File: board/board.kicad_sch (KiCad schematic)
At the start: 34 parts, among them J1 Conn_01x25_Socket, J2 Conn_01x25_Socket, J5 PJ-320B, J6 Screw_Terminal_01x02, J7 Screw_Terminal_01x02, J8 Screw_Terminal_01x02

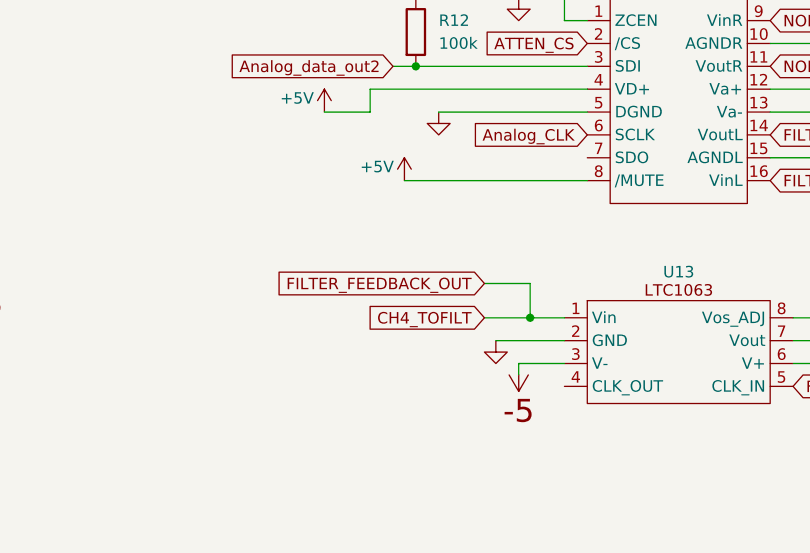
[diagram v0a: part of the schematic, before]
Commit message: connection successful message + add resistor to filter feedback loop
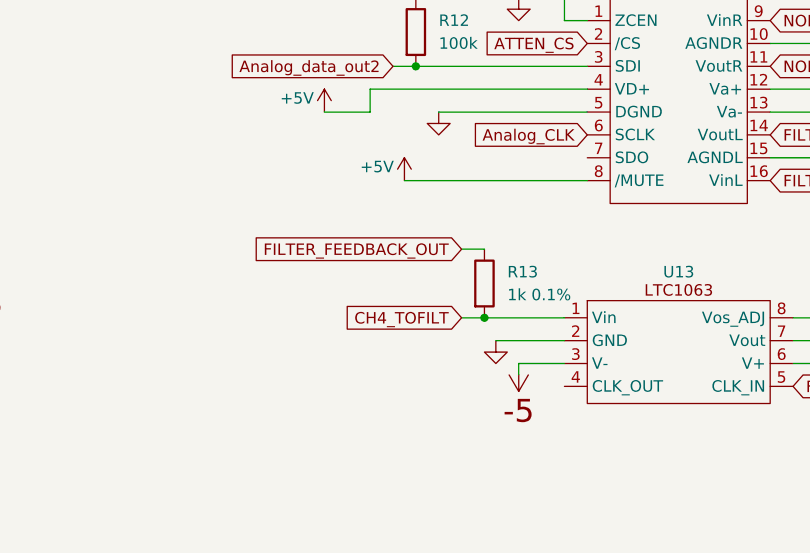
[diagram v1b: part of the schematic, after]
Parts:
- added R13: 1k_0603_0.1%, 4ms_Resistor:R_0603, symbol 4ms_Resistor:1k_0603_0.1%
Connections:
- net CH4_TOFILT: now also R13.2; no longer U10.14 (VoutL)
- new net FILTER_FEEDBACK_OUT: R13.1, U10.14 (VoutL)
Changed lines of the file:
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@@
 	)
 	(junction
-		(at 133.35 247.65)
-		(diameter 0)
-		(color 0 0 0 0)
-	)
-	(junction
 		(at 120.65 219.71)
 		(diameter 0)
@@
 	)
 	(junction
+		(at 128.27 247.65)
+		(diameter 0)
+		(color 0 0 0 0)
+	)
+	(junction
 		(at 229.87 236.22)
 		(diameter 0)
@@
 	(wire
 		(pts
-			(xy 128.27 247.65) (xy 133.35 247.65)
+			(xy 125.73 247.65) (xy 128.27 247.65)
 		)
 		(stroke
@@
 	(wire
 		(pts
+			(xy 128.27 247.65) (xy 137.16 247.65)
+		)
+		(stroke
+			(width 0)
+			(type default)
+		)
+	)
+	(wire
+		(pts
 			(xy 129.54 58.42) (xy 129.54 59.69)
 		)
@@
 	(wire
 		(pts
-			(xy 133.35 243.84) (xy 133.35 247.65)
-		)
-		(stroke
-			(width 0)
-			(type default)
-		)
-	)
-	(wire
-		(pts
 			(xy 82.55 175.26) (xy 82.55 177.8)
 		)
@@
 	(wire
 		(pts
-			(xy 133.35 247.65) (xy 137.16 247.65)
-		)
-		(stroke
-			(width 0)
-			(type default)
-		)
-	)
-	(wire
-		(pts
 			(xy 134.62 139.7) (xy 137.16 139.7)
 		)
@@
 	(wire
 		(pts
-			(xy 128.27 243.84) (xy 133.35 243.84)
+			(xy 125.73 240.03) (xy 128.27 240.03)
 		)
 		(stroke
@@
 	(global_label "CH4_TOFILT"
 		(shape input)
-		(at 128.27 247.65 180)
+		(at 125.73 247.65 180)
 		(fields_autoplaced yes)
 		(effects
@@
 		)
 		(property "Intersheetrefs" "${INTERSHEET_REFS}"
-			(at 114.52 247.65 0)
+			(at 111.98 247.65 0)
 			(effects
 				(font
@@
 	(global_label "FILTER_FEEDBACK_OUT"
 		(shape input)
-		(at 128.27 243.84 180)
+		(at 125.73 240.03 180)
 		(fields_autoplaced yes)
 		(effects
@@
 		)
 		(property "Intersheetrefs" "${INTERSHEET_REFS}"
-			(at 104.0577 243.84 0)
+			(at 101.5177 240.03 0)
 			(effects
 				(font
@@
 					(unit 1)
 				)
+			)
+		)
+	)
+	(symbol
+		(lib_id "4ms_Resistor:1k_0603_0.1%")
+		(at 128.27 243.84 0)
+		(unit 1)
+		(exclude_from_sim no)
+		(in_bom yes)
+		(on_board yes)
+		(dnp no)
+		(fields_autoplaced yes)
+		(property "Reference" "R13"
+			(at 130.81 242.5699 0)
+			(effects
+				(font
+					(size 1.27 1.27)
+				)
+				(justify left)
+			)
+		)
+		(property "Value" "1k_0603_0.1%"
+			(at 125.73 243.84 90)
+			(effects
+				(font
+					(size 1.27 1.27)
+				)
+				(hide yes)
+			)
+		)
+		(property "Footprint" "4ms_Resistor:R_0603"
+			(at 125.73 256.54 0)
+			(effects
+				(font
+					(size 1.27 1.27)
+				)
+				(justify left)
+				(hide yes)
+			)
+		)
+		(property "Datasheet" ""
+			(at 128.27 243.84 0)
+			(effects
+				(font
+					(size 1.27 1.27)
+				)
+				(hide yes)
+			)
+		)
+		(property "Description" "1k, 0.1%, 1/16W, 0603 25ppm"
+			(at 128.27 243.84 0)
+			(effects
+				(font
+					(size 1.27 1.27)
+				)
+				(hide yes)
+			)
+		)
+		(property "Display" "1k 0.1%"
+			(at 130.81 245.1099 0)
+			(effects
+				(font
+					(size 1.27 1.27)
+				)
+				(justify left)
+			)
+		)
+		(property "Specifications" "1k, 0.1%, 1/16W, 0603, 25ppm"
+			(at 125.73 251.714 0)
+			(effects
+				(font
+					(size 1.27 1.27)
+				)
+				(justify left)
+				(hide yes)
+			)
+		)
+		(property "Manufacturer" "Panasonic"
+			(at 125.73 253.238 0)
+			(effects
+				(font
+					(size 1.27 1.27)
+				)
+				(justify left)
+				(hide yes)
+			)
+		)
+		(property "Part Number" "ERA-3AEB102V"
+			(at 125.73 254.762 0)
+			(effects
+				(font
+					(size 1.27 1.27)
+				)
+				(justify left)
+				(hide yes)
+			)
+		)
+		(property "Manufacturer 2" "Yageo"
+			(at 126.365 258.445 0)
+			(effects
+				(font
+					(size 1.27 1.27)
+				)
+				(justify left)
+				(hide yes)
+			)
+		)
+		(property "Part Number 2" "RT0603BRD071KL"
+			(at 126.365 260.35 0)
+			(effects
+				(font
+					(size 1.27 1.27)
+				)
+				(justify left)
+				(hide yes)
+			)
+		)
+		(property "JLCPCB ID" "C54019"
+			(at 126.365 260.35 0)
+			(effects
+				(font
+					(size 1.27 1.27)
+				)
+				(justify left)
+				(hide yes)
+			)
+		)
+		(pin "1"
+		)
+		(pin "2"
+		)
+		(instances
+			(project "board"
+				(path "/e8cec806-e837-4d6f-b166-2de75a563bd6"
+					(reference "R13")
+					(unit 1)
+				)

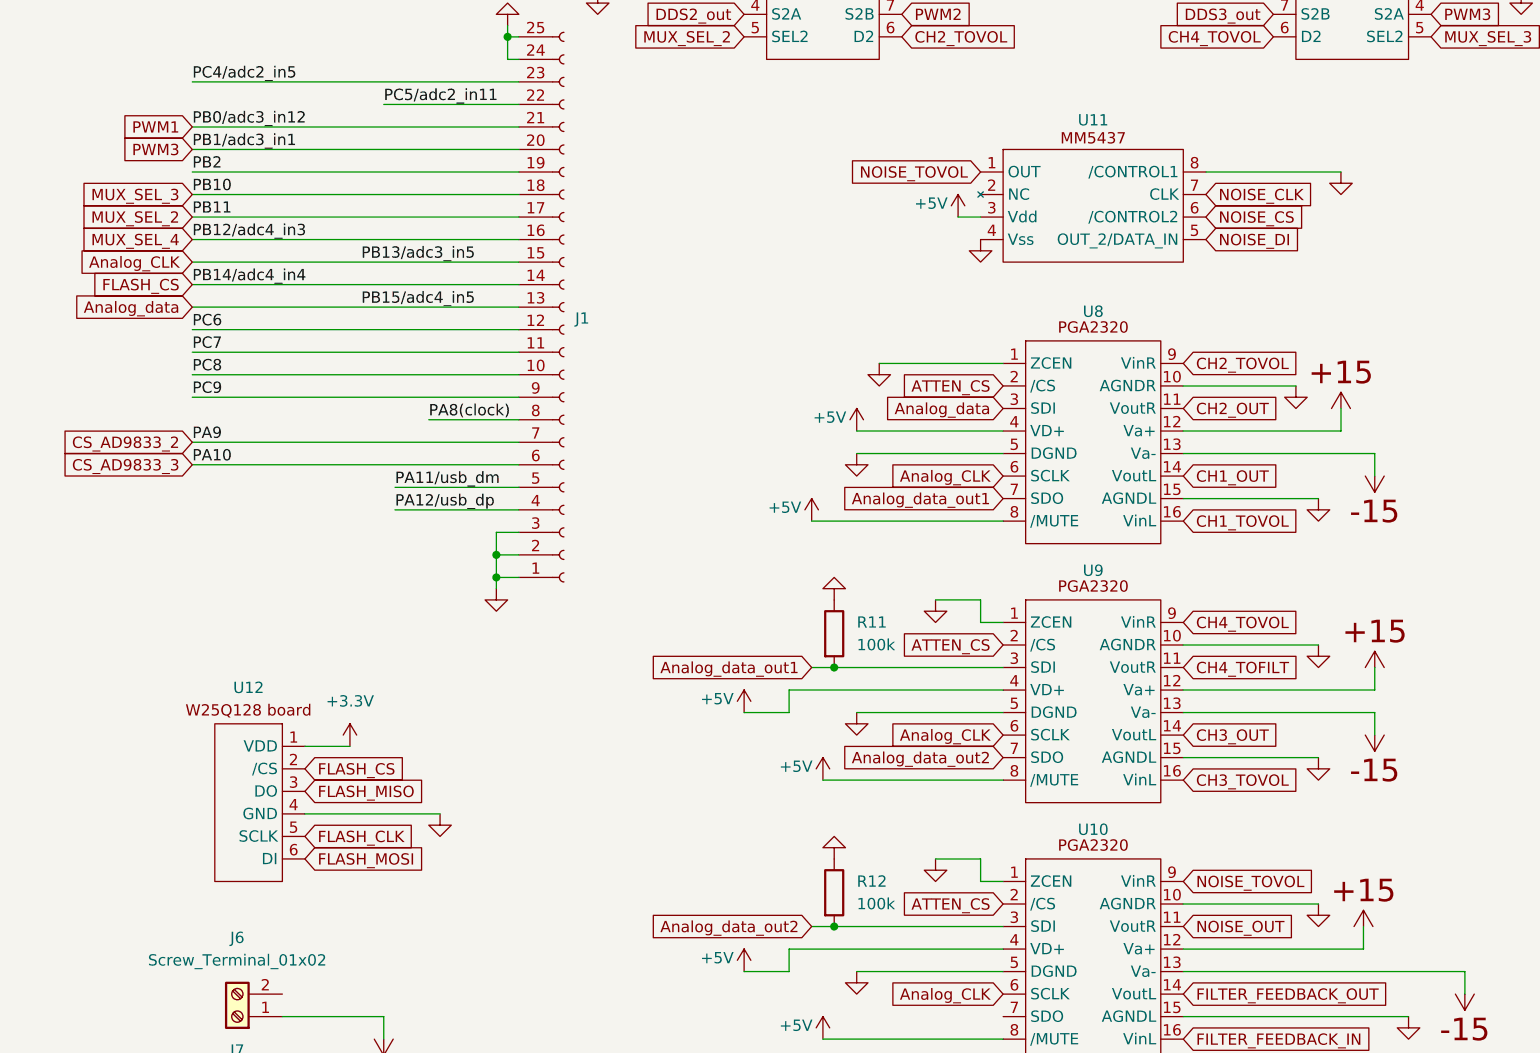
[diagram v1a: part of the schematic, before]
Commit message: add noise clock source and mute function control
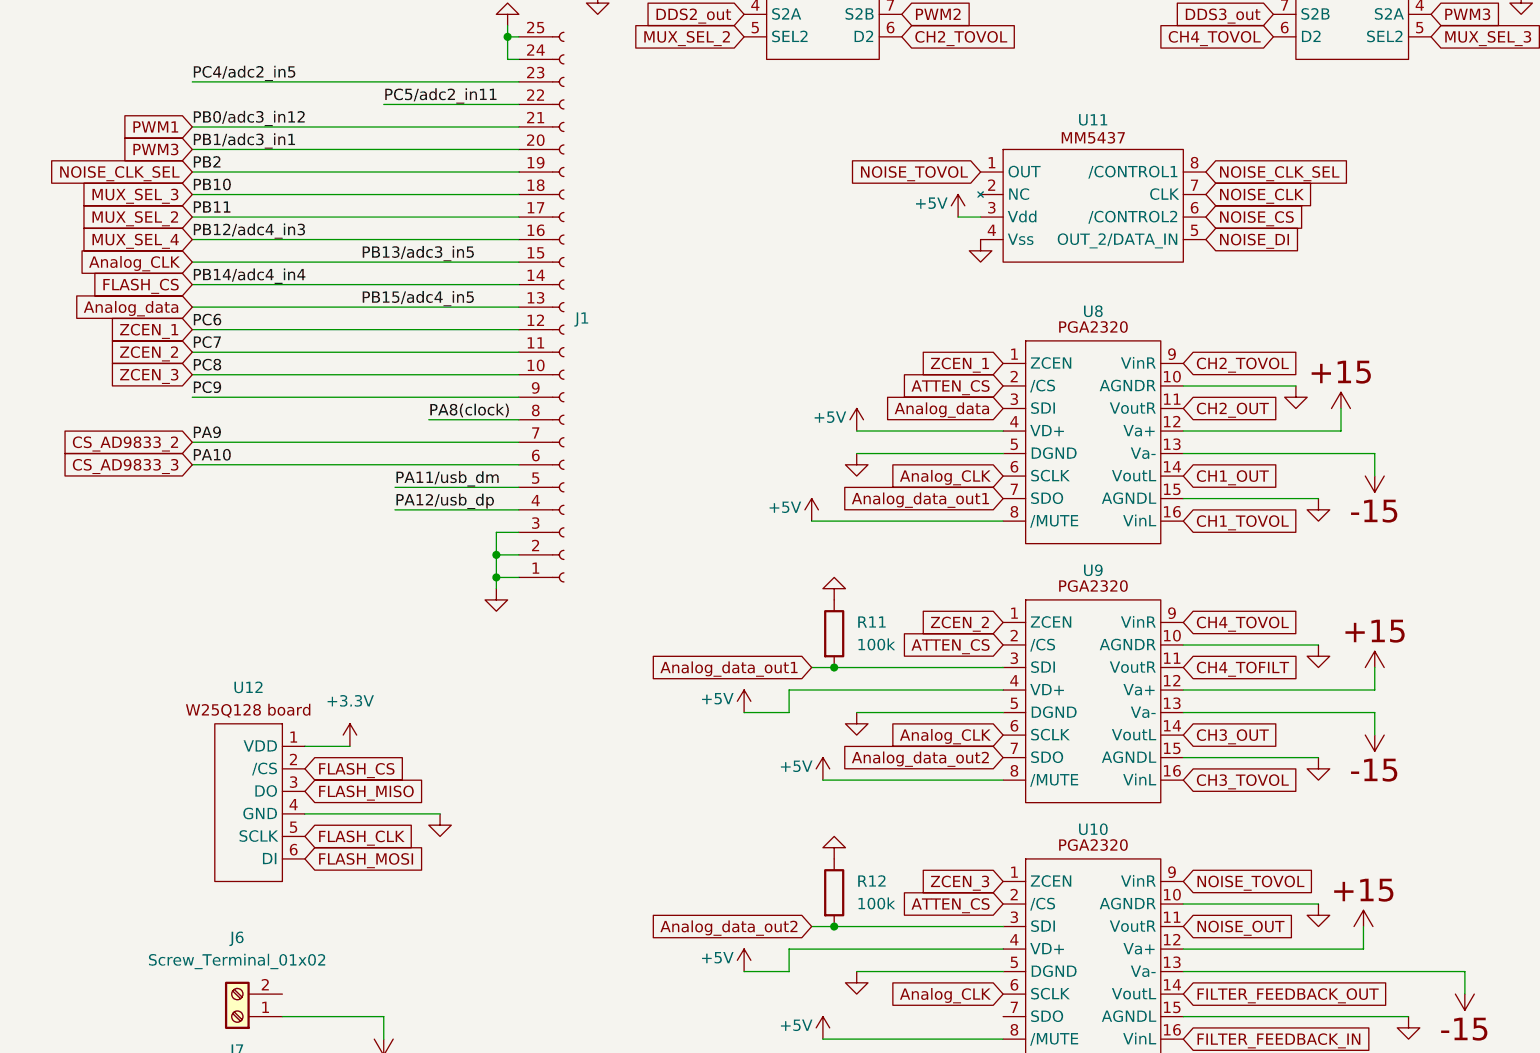
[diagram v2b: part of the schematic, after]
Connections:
- net GND: no longer U10.1 (ZCEN), U11.8 (/CONTROL1), U8.1 (ZCEN), U9.1 (ZCEN)
- net PB2 renamed NOISE_CLK_SEL
- net NOISE_CLK_SEL: now also U11.8 (/CONTROL1)
- net PC6 renamed ZCEN_1
- net ZCEN_1: now also U8.1 (ZCEN)
- net PC7 renamed ZCEN_2
- net ZCEN_2: now also U9.1 (ZCEN)
- net PC8 renamed ZCEN_3
- net ZCEN_3: now also U10.1 (ZCEN)
